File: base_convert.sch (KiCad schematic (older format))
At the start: 10 parts, among them J1 ISP, J2 Extra, Q1 Q_PMOS_GSD, SW2 SELECT, U1 MSP430FR2033IPMR

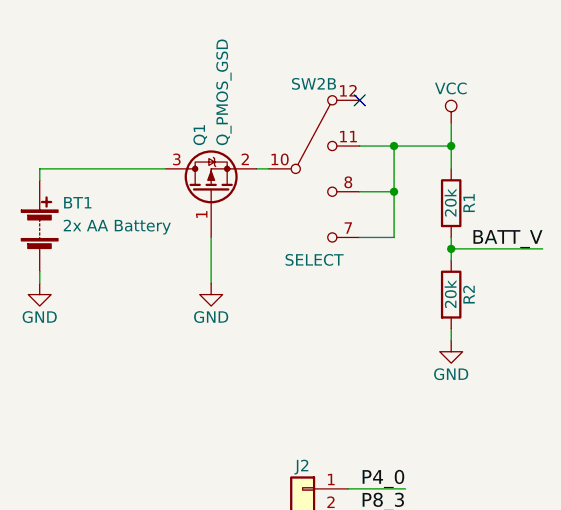
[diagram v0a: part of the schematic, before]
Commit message: update switch fields
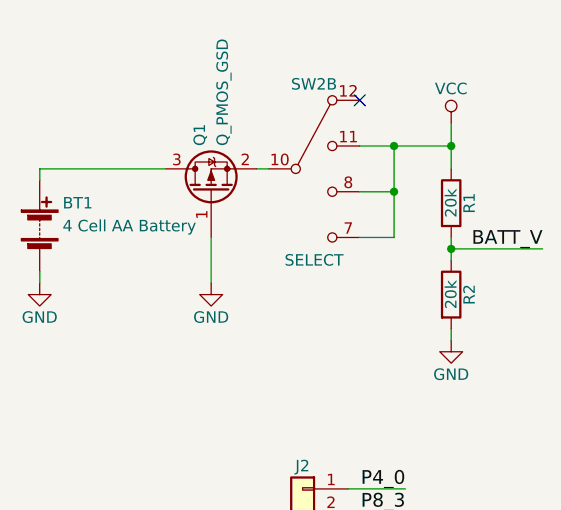
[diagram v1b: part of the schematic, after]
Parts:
- BT1: value 2x AA Battery -> 4 Cell AA Battery; footprint MPD:BC2AAPC -> MPD:BC4AAPC; Description HOLDER BATT 2-AA CELLS PC MNT -> HOLDER BATT 4-AA CELLS PC MNT; Mfg Part Number BC2AAPC -> BC4AAPC

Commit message: update pmos fields
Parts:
- J2: Description NONE -> (none); Manufacture NONE -> (none); Mfg Part Number NONE -> (none); Package NONE -> (none)
- Q1: Description (none) -> MOSFET P-CH 20V 5.3A SOT-23; Manufacture (none) -> Vishay Siliconix; Mfg Part Number (none) -> SI2323DDS-T1-GE3; Package (none) -> SOT-23
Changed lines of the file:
@@
 F 1 "Q_PMOS_GSD" H 1950 1150 50  0000 L CNN
 F 2 "TO_SOT_Packages_SMD:SOT-23" H 1950 1300 50  0001 C CNN
-F 3 "" H 1750 1200 50  0001 C CNN
+F 3 "http://www.vishay.com/docs/64004/si2323dds.pdf" H 1750 1200 50  0001 C CNN
+F 4 "Vishay Siliconix" H 1950 1350 50  0001 C CNN "Manufacture"
+F 5 "SI2323DDS-T1-GE3" H 1950 1350 50  0001 C CNN "Mfg Part Number"
+F 6 "SOT-23" H 1950 1350 50  0001 C CNN "Package"
+F 7 "MOSFET P-CH 20V 5.3A SOT-23" H 1950 1350 50  0001 C CNN "Description"
 	1    1750 1200
 	0    -1   -1   0
@@
 F 2 "Pin_Headers:Pin_Header_Straight_1x04_Pitch2.54mm" H 2150 2600 50  0001 C CNN
 F 3 "" H 2150 2600 50  0001 C CNN
-F 4 "NONE" H 2150 2600 60  0001 C CNN "Description"
-F 5 "NONE" H 2150 2600 60  0001 C CNN "Manufacture"
-F 6 "NONE" H 2150 2600 60  0001 C CNN "Mfg Part Number"
-F 7 "NONE" H 2150 2600 60  0001 C CNN "Package"
 	1    2150 2600
 	-1   0    0    -1

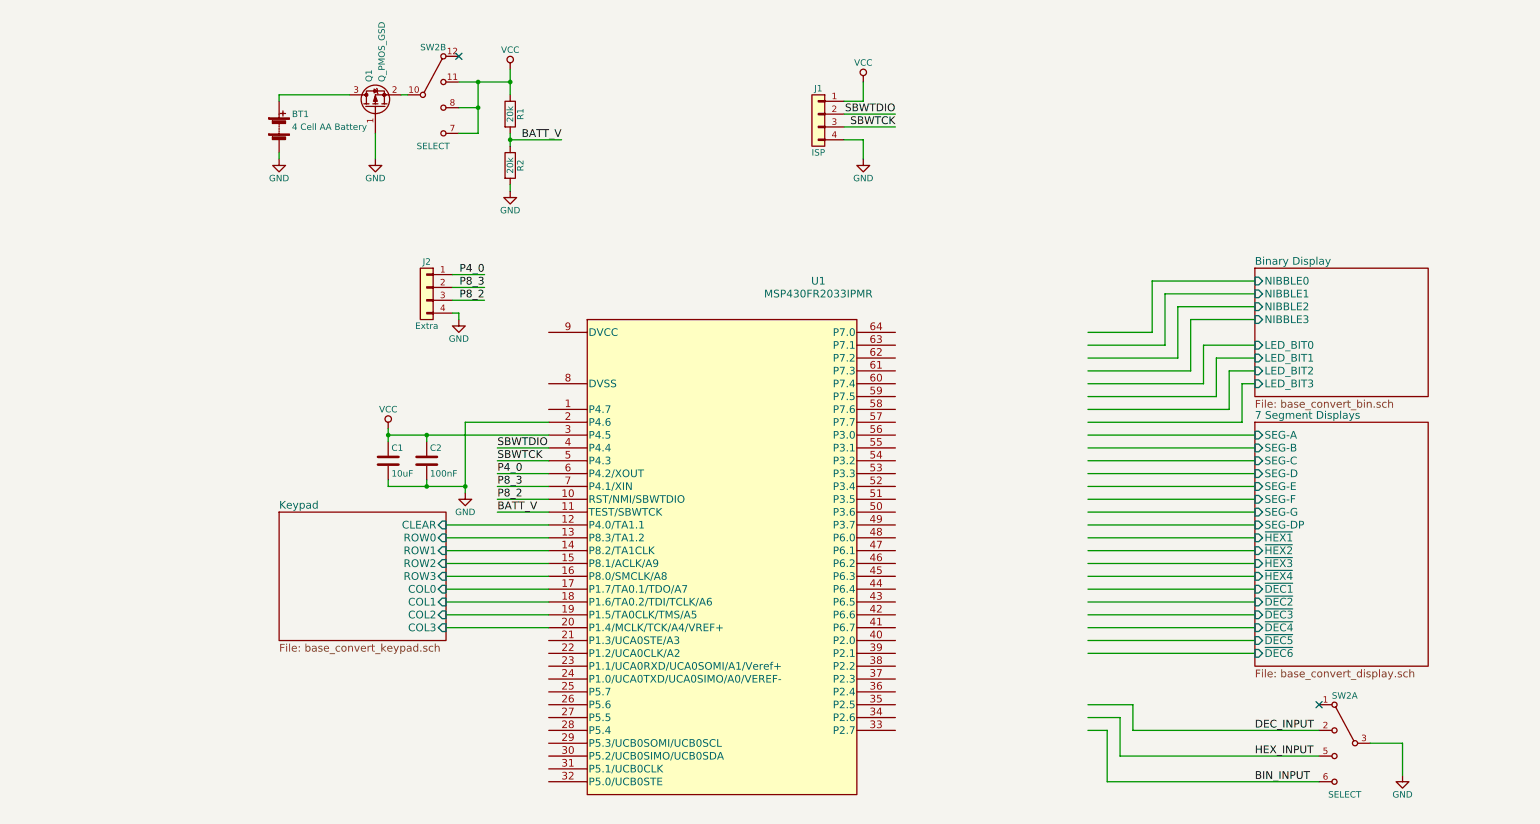
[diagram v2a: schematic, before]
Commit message: add 3v3 ldo
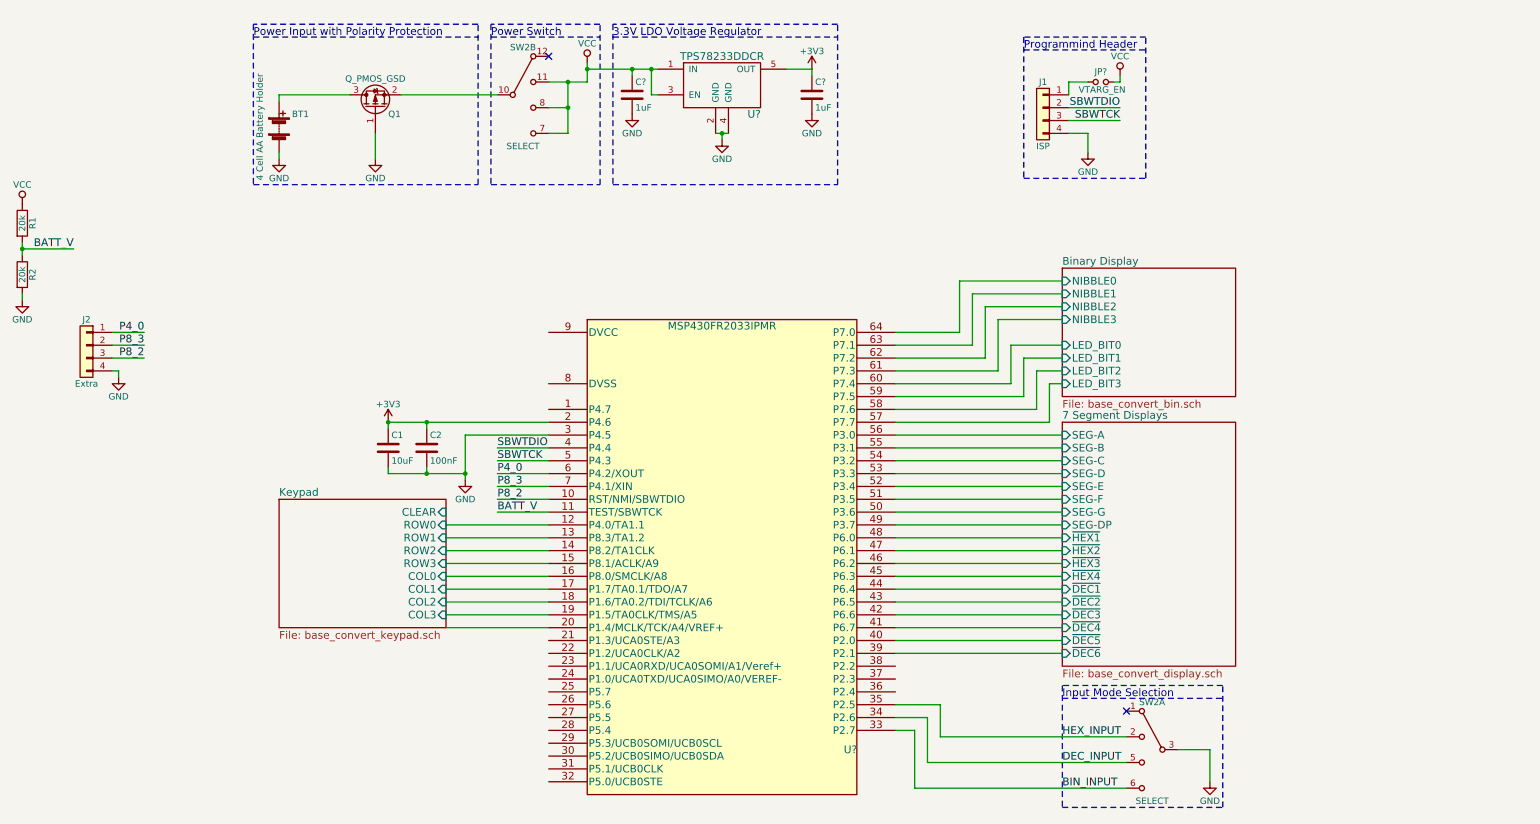
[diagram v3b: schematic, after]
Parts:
- removed U1: MSP430FR2033IPMR, Housings_QFP:LQFP-64_10x10mm_Pitch0.5mm, symbol MSP430FR2033IPMR
- added C? (x2): 1uF, symbol C
- added JP?: VTARG_EN, symbol Jumper_NO_Small
- added U?: TPS78233DDCR, symbol TPS782
- added U?: MSP430FR2033IPMR, PM64, symbol MSP430FR2033IPMR
- BT1: value 4 Cell AA Battery -> 4 Cell AA Battery Holder
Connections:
- net labels added: +3V3
- wire segments 100 -> 120
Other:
- note added: "3.3V LDO Voltage Regulator"
- note added: "Input Mode Selection"
- note added: "Power Input with Polarity Protection"
- note added: "Power Switch"
- note added: "Programmind Header"
- moved on the sheet: C1, C2, J1, J2, R1, R2, SW2A, SW2B

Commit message: update msp430 symbol for cleaner schematic
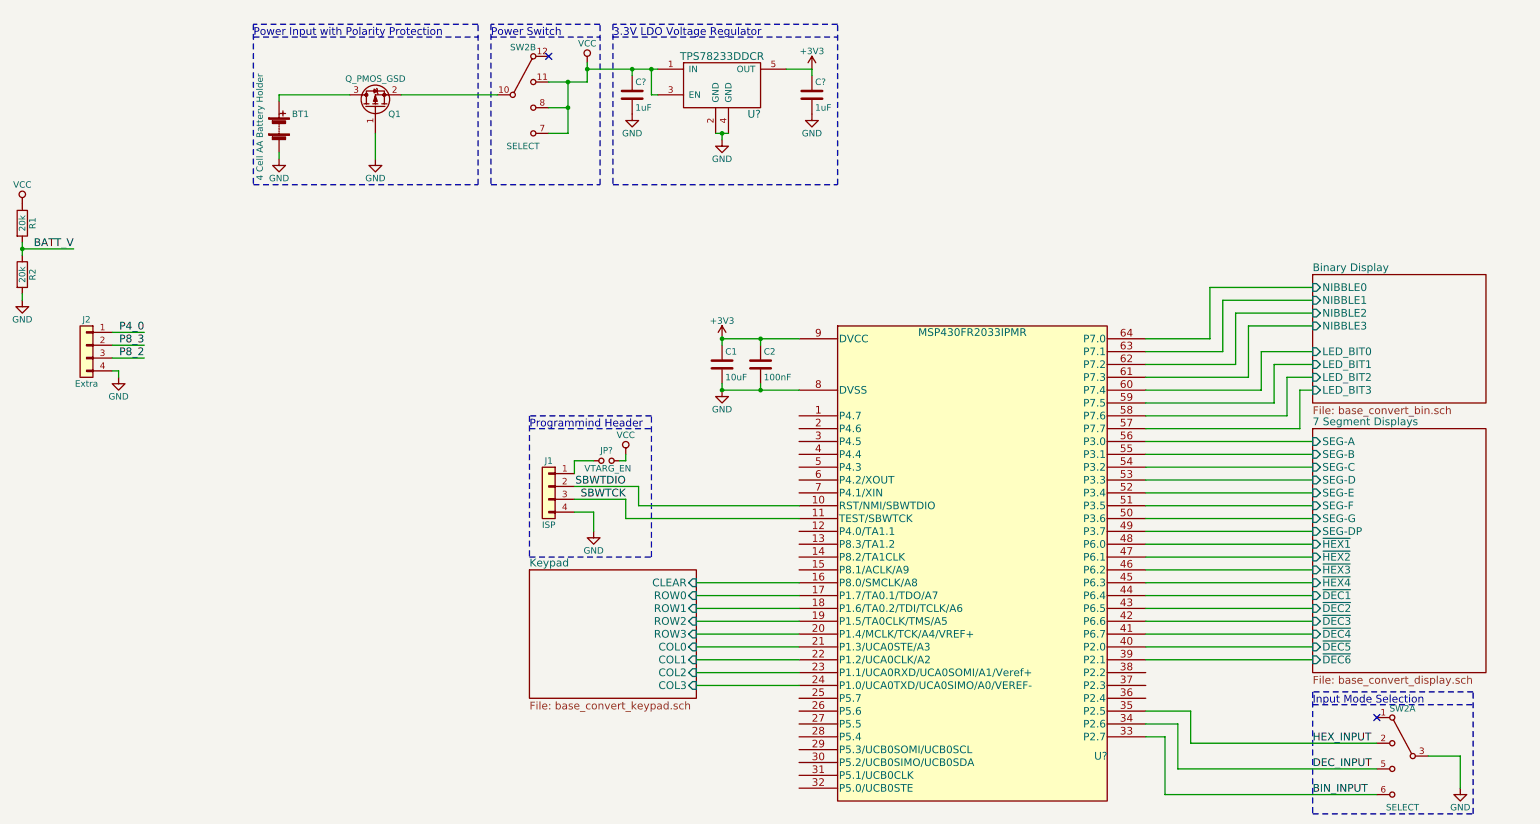
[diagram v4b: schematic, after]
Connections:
- net +3V3: now also U?.9 (DVCC); no longer U?.2 (P4.6)
- net BATT_V: no longer U?.11 (TEST/SBWTCK)
- net GND: now also U?.8 (DVSS); no longer U?.3 (P4.5)
- net Keypad/CLEAR: now also U?.16 (P8.0/SMCLK/A8)
- net Keypad/COL0: now also U?.21 (P1.3/UCA0STE/A3); no longer U?.16 (P8.0/SMCLK/A8)
- net Keypad/COL1: now also U?.22 (P1.2/UCA0CLK/A2); no longer U?.17 (P1.7/TA0.1/TDO/A7)
- net Keypad/COL2: now also U?.23 (P1.1/UCA0RXD/UCA0SOMI/A1/Veref+); no longer U?.18 (P1.6/TA0.2/TDI/TCLK/A6)
- net Keypad/COL3: now also U?.24 (P1.0/UCA0TXD/UCA0SIMO/A0/VEREF-); no longer U?.19 (P1.5/TA0CLK/TMS/A5)
- net Keypad/ROW0: now also U?.17 (P1.7/TA0.1/TDO/A7); no longer U?.12 (P4.0/TA1.1)
- net Keypad/ROW1: now also U?.18 (P1.6/TA0.2/TDI/TCLK/A6); no longer U?.13 (P8.3/TA1.2)
- net Keypad/ROW2: now also U?.19 (P1.5/TA0CLK/TMS/A5); no longer U?.14 (P8.2/TA1CLK)
- net Keypad/ROW3: now also U?.20 (P1.4/MCLK/TCK/A4/VREF+); no longer U?.15 (P8.1/ACLK/A9)
- net P4_0: no longer U?.6 (P4.2/XOUT)
- net P8_2: no longer U?.10 (RST/NMI/SBWTDIO)
- net P8_3: no longer U?.7 (P4.1/XIN)
- net SBWTCK: now also U?.11 (TEST/SBWTCK); no longer U?.5 (P4.3)
- net SBWTDIO: now also U?.10 (RST/NMI/SBWTDIO); no longer U?.4 (P4.4)
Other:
- moved on the sheet: C1, C2, J1, JP?, SW2A, U?

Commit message: modify batery monitor divider
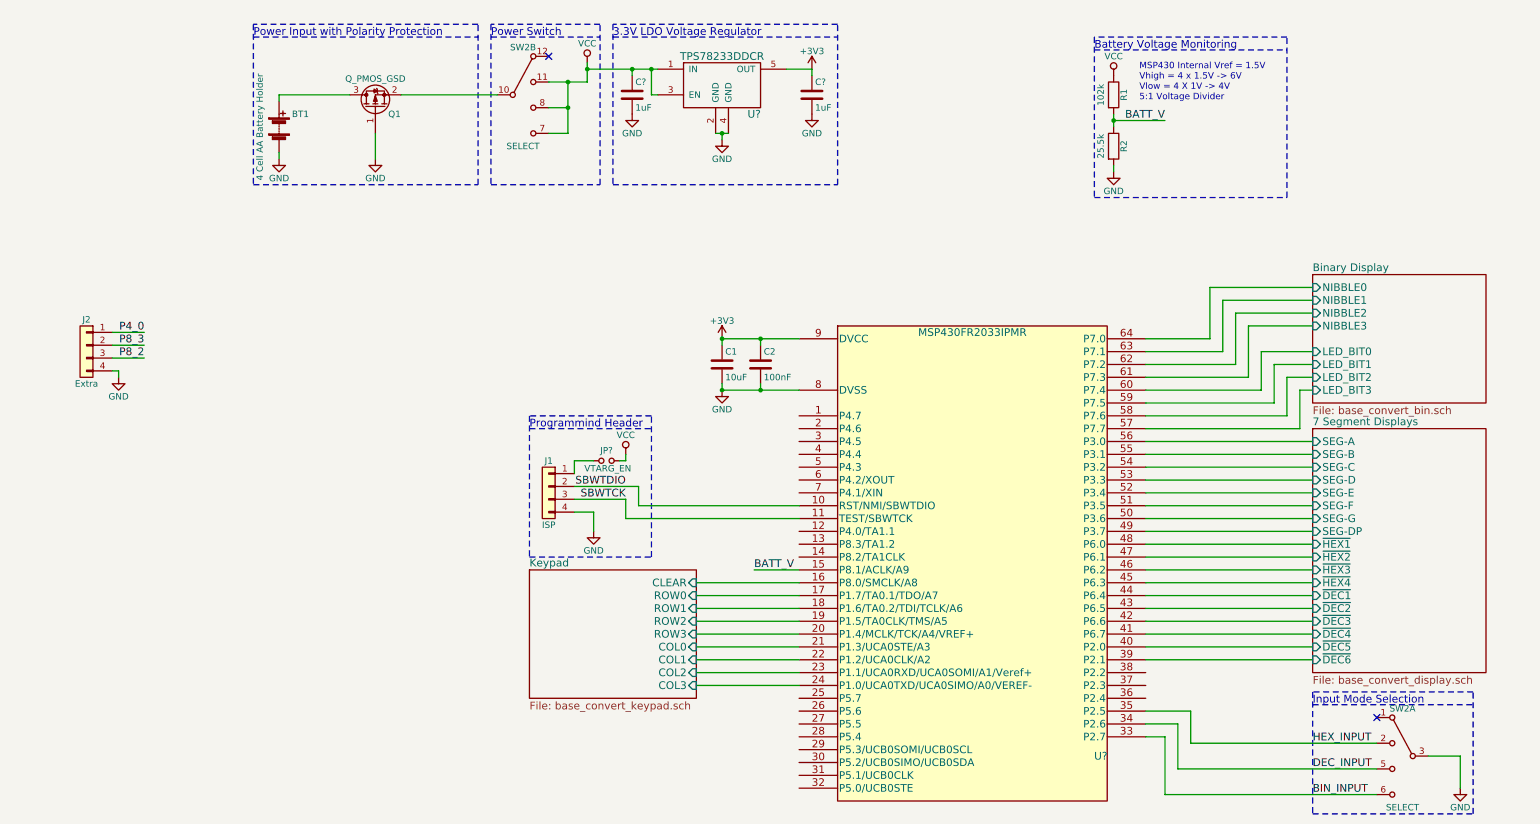
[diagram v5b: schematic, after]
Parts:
- R1: value 20k -> 102k; Description (none) -> NONE; Manufacture (none) -> NONE; Mfg Part Number (none) -> NONE; Package (none) -> NONE
- R2: value 20k -> 25.5k; Description (none) -> NONE; Manufacture (none) -> NONE; Mfg Part Number (none) -> NONE; Package (none) -> NONE
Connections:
- net BATT_V: now also U?.15 (P8.1/ACLK/A9)
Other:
- note added: "Battery Voltage Monitoring"
- note added: "MSP430 Internal Vref = 1.5V\nVhigh = 4 x 1.5V -> 6V\nVlow = 4 X 1V -> 4V\n5:1 Voltage Divider"
- moved on the sheet: R1, R2
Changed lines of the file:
@@
 L R R1
 U 1 1 5AF2F1FC
-P -1000 2100
-F 0 "R1" V -920 2100 50  0000 C CNN
-F 1 "20k" V -1000 2100 50  0000 C CNN
-F 2 "Resistors_SMD:R_0805" V -1070 2100 50  0001 C CNN
-F 3 "" H -1000 2100 50  0001 C CNN
-	1    -1000 2100
+P 7500 1100
+F 0 "R1" V 7580 1100 50  0000 C CNN
+F 1 "102k" V 7400 1100 50  0000 C CNN
+F 2 "Resistors_SMD:R_0805" V 7430 1100 50  0001 C CNN
+F 3 "" H 7500 1100 50  0001 C CNN
+F 4 "NONE" H 7500 1100 60  0001 C CNN "Manufacture"
+F 5 "NONE" H 7500 1100 60  0001 C CNN "Mfg Part Number"
+F 6 "NONE" H 7500 1100 60  0001 C CNN "Package"
+F 7 "NONE" H 7500 1100 60  0001 C CNN "Description"
+	1    7500 1100
 	1    0    0    -1
 $EndComp
@@
 L R R2
 U 1 1 5AF2FAFB
-P -1000 2500
-F 0 "R2" V -920 2500 50  0000 C CNN
-F 1 "20k" V -1000 2500 50  0000 C CNN
-F 2 "Resistors_SMD:R_0805" V -1070 2500 50  0001 C CNN
-F 3 "" H -1000 2500 50  0001 C CNN
-	1    -1000 2500
+P 7500 1500
+F 0 "R2" V 7580 1500 50  0000 C CNN
+F 1 "25.5k" V 7400 1500 50  0000 C CNN
+F 2 "Resistors_SMD:R_0805" V 7430 1500 50  0001 C CNN
+F 3 "" H 7500 1500 50  0001 C CNN
+F 4 "NONE" H 7500 1500 60  0001 C CNN "Manufacture"
+F 5 "NONE" H 7500 1500 60  0001 C CNN "Mfg Part Number"
+F 6 "NONE" H 7500 1500 60  0001 C CNN "Package"
+F 7 "NONE" H 7500 1500 60  0001 C CNN "Description"
+	1    7500 1500
 	1    0    0    -1
 $EndComp
@@
 L GND #PWR7
 U 1 1 5AF3048A
-P -1000 2700
-F 0 "#PWR7" H -1000 2450 50  0001 C CNN
-F 1 "GND" H -1000 2550 50  0000 C CNN
-F 2 "" H -1000 2700 50  0001 C CNN
-F 3 "" H -1000 2700 50  0001 C CNN
-	1    -1000 2700
+P 7500 1700
+F 0 "#PWR7" H 7500 1450 50  0001 C CNN
+F 1 "GND" H 7500 1550 50  0000 C CNN
+F 2 "" H 7500 1700 50  0001 C CNN
+F 3 "" H 7500 1700 50  0001 C CNN
+	1    7500 1700
 	1    0    0    -1
 $EndComp
@@
 Text Label 9050 6550 0    60   ~ 0
 BIN_INPUT
-Text Label -600 2300 2    60   ~ 0
+Text Label 7900 1300 2    60   ~ 0
 BATT_V
 Text Label 3700 4150 2    60   ~ 0
@@
 L VCC #PWR?
 U 1 1 5B28B1DA
-P -1000 1950
-F 0 "#PWR?" H -1000 1800 50  0001 C CNN
-F 1 "VCC" H -1000 2100 50  0000 C CNN
-F 2 "" H -1000 1950 50  0001 C CNN
-F 3 "" H -1000 1950 50  0001 C CNN
-	1    -1000 1950
+P 7500 950
+F 0 "#PWR?" H 7500 800 50  0001 C CNN
+F 1 "VCC" H 7500 1100 50  0000 C CNN
+F 2 "" H 7500 950 50  0001 C CNN
+F 3 "" H 7500 950 50  0001 C CNN
+	1    7500 950
 	1    0    0    -1
 $EndComp
@@
 	1750 1600 1750 1400
 Wire Wire Line
-	4450 3000 4750 3000
-Wire Wire Line
-	4750 3000 5050 3000
+	4450 3000 5050 3000
 Wire Wire Line
 	4450 3000 4450 3050
@@
 	4450 3350 4450 3400
 Wire Wire Line
-	4450 3400 4750 3400
-Wire Wire Line
-	4750 3400 5050 3400
+	4450 3400 5050 3400
 Wire Wire Line
 	1000 1100 1550 1100
@@
 	10200 6250 9950 6250
 Wire Wire Line
-	-1000 2700 -1000 2650
-Wire Wire Line
-	-1000 2250 -1000 2300
-Wire Wire Line
-	-1000 2300 -1000 2350
-Wire Wire Line
-	-1000 2300 -600 2300
+	7500 1700 7500 1650
+Wire Wire Line
+	7500 1250 7500 1350
+Wire Wire Line
+	7500 1300 7900 1300
 Wire Wire Line
 	3300 4350 3450 4350
@@
 Connection ~ 4750 3400
 Connection ~ 4450 3000
-Connection ~ -1000 2300
+Connection ~ 7500 1300
 Connection ~ 3250 1000
 Connection ~ 3250 1200
@@
 	5150 900  5150 950
 Wire Wire Line
-	4400 1400 4450 1400
-Wire Wire Line
-	4450 1400 4500 1400
+	4400 1400 4500 1400
 Wire Wire Line
 	4450 1450 4450 1400
 Connection ~ 4450 1400
 Wire Wire Line
-	3250 1000 3250 1200
-Wire Wire Line
-	3250 1200 3250 1400
+	3250 1000 3250 1400
 Wire Wire Line
 	3300 4050 3300 3950
@@
 	2950 3700 3900 3700
 Wire Wire Line
-	3400 1000 3250 1000
-Wire Wire Line
-	3250 1000 3100 1000
-Wire Wire Line
-	3400 900  3750 900
-Wire Wire Line
-	3750 900  3900 900
-Wire Wire Line
-	3900 900  3950 900
+	3400 1000 3100 1000
+Wire Wire Line
+	3400 900  3950 900
 Wire Notes Line
 	3600 550  3600 1800
@@
 	2650 650  3500 650
 Wire Wire Line
-	3400 850  3400 900
-Wire Wire Line
-	3400 900  3400 1000
+	3400 850  3400 1000
 Connection ~ 3400 900
 Connection ~ 4450 3400
@@
 Wire Wire Line
 	3800 4300 5050 4300
+Text Notes 7700 1150 0    50   ~ 0
+MSP430 Internal Vref = 1.5V\nVhigh = 4 x 1.5V -> 6V\nVlow = 4 X 1V -> 4V\n5:1 Voltage Divider
+Text Notes 7350 750  0    60   ~ 0
+Battery Voltage Monitoring
+Wire Notes Line
+	7350 650  7350 1900
+Wire Notes Line
+	7350 1900 8850 1900
+Wire Notes Line
+	8850 1900 8850 650
+Wire Notes Line
+	8850 650  7350 650
+Wire Notes Line
+	7350 750  8850 750
+Text Label 4700 4800 0    60   ~ 0
+BATT_V
+Wire Wire Line
+	4700 4800 5050 4800
 $EndSCHEMATC
